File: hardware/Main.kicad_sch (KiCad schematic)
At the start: 1 part

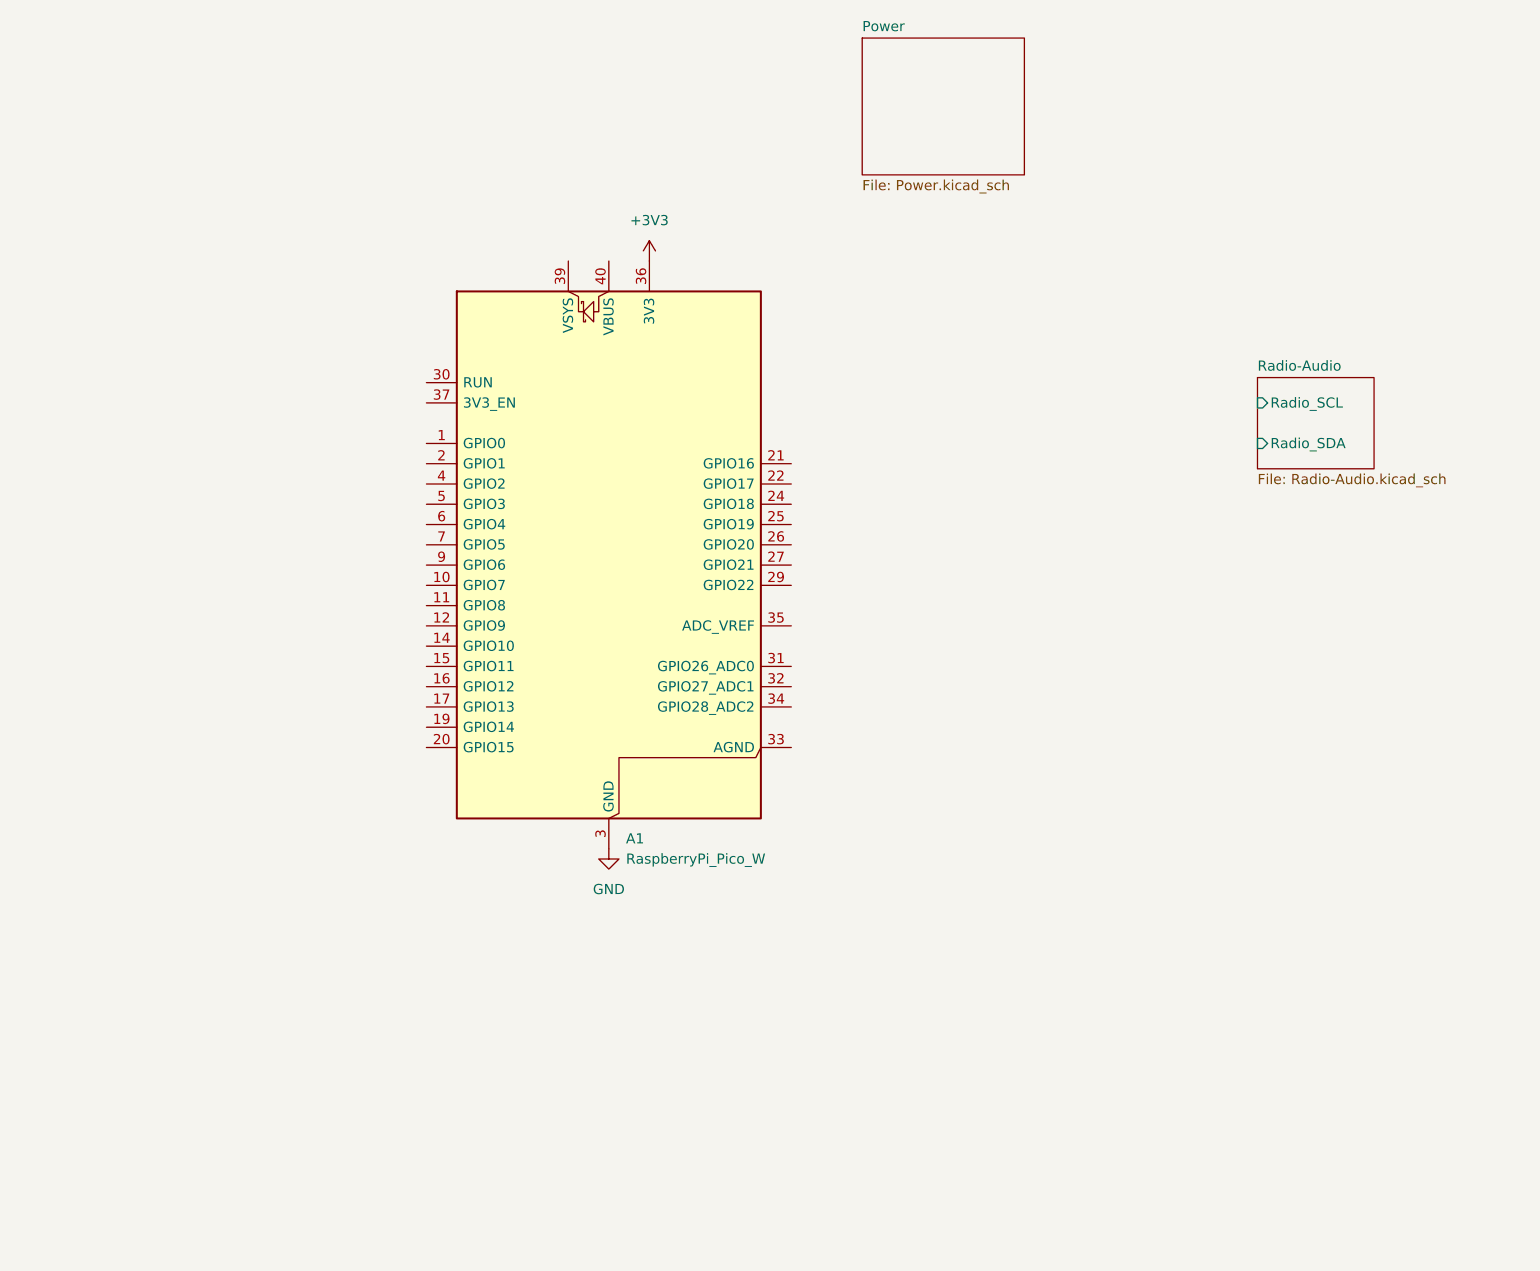
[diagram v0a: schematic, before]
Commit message: Added Radio Module to circuit
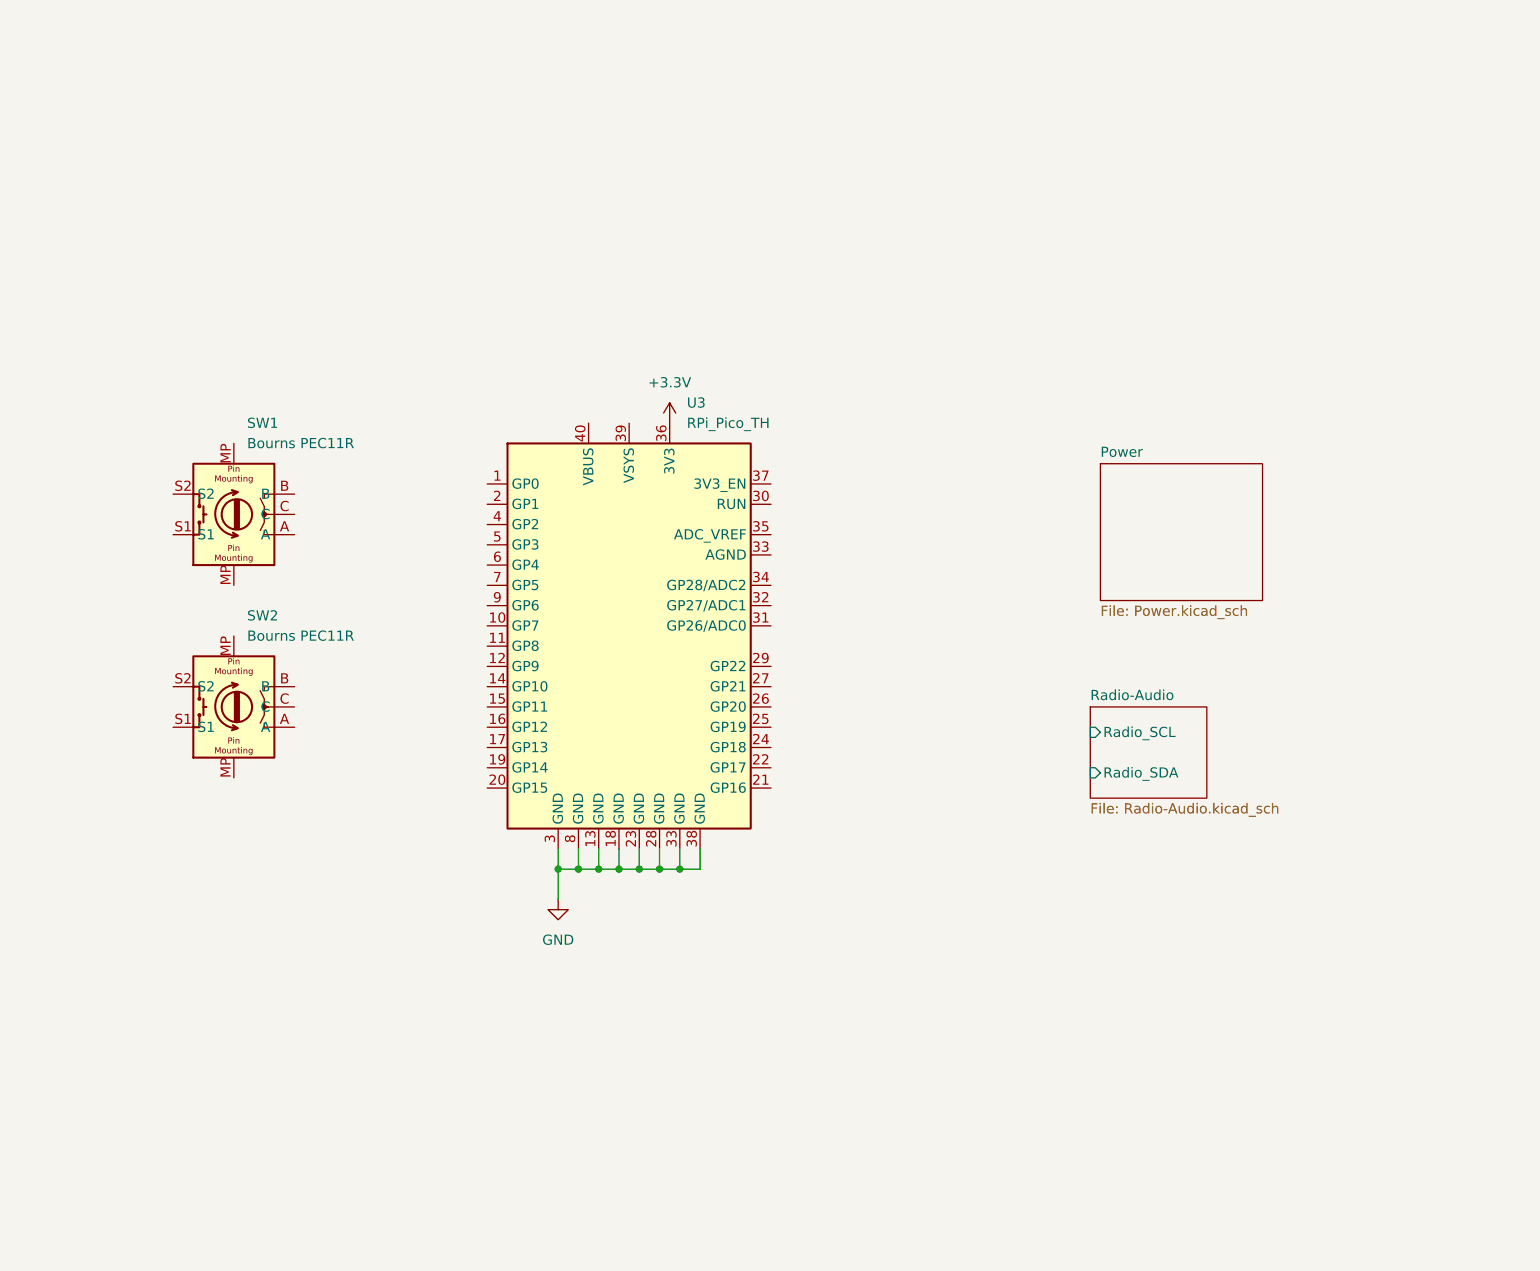
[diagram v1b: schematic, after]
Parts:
- removed A1: RaspberryPi_Pico_W, Module:RaspberryPi_Pico_Common_SMD, symbol MCU_Module:RaspberryPi_Pico_W
- added SW1, SW2: Bourns PEC11R, Rotary_Encoder:RotaryEncoder_Alps_EC12E-Switch_Vertical_H20mm, symbol ECE:Bourns PEC11R
- added U3: RPi_Pico_TH, ECE:RPi_Pico_TH, symbol ECE:RPi_Pico_TH
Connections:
- net GND: now also U3.13 (GND), U3.18 (GND), U3.23 (GND), U3.28 (GND), U3.3 (GND), U3.33 (AGND), U3.38 (GND), U3.8 (GND)
- new net +3.3V: U3.36 (3V3)

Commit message: Updated Encoder Circuit/Code
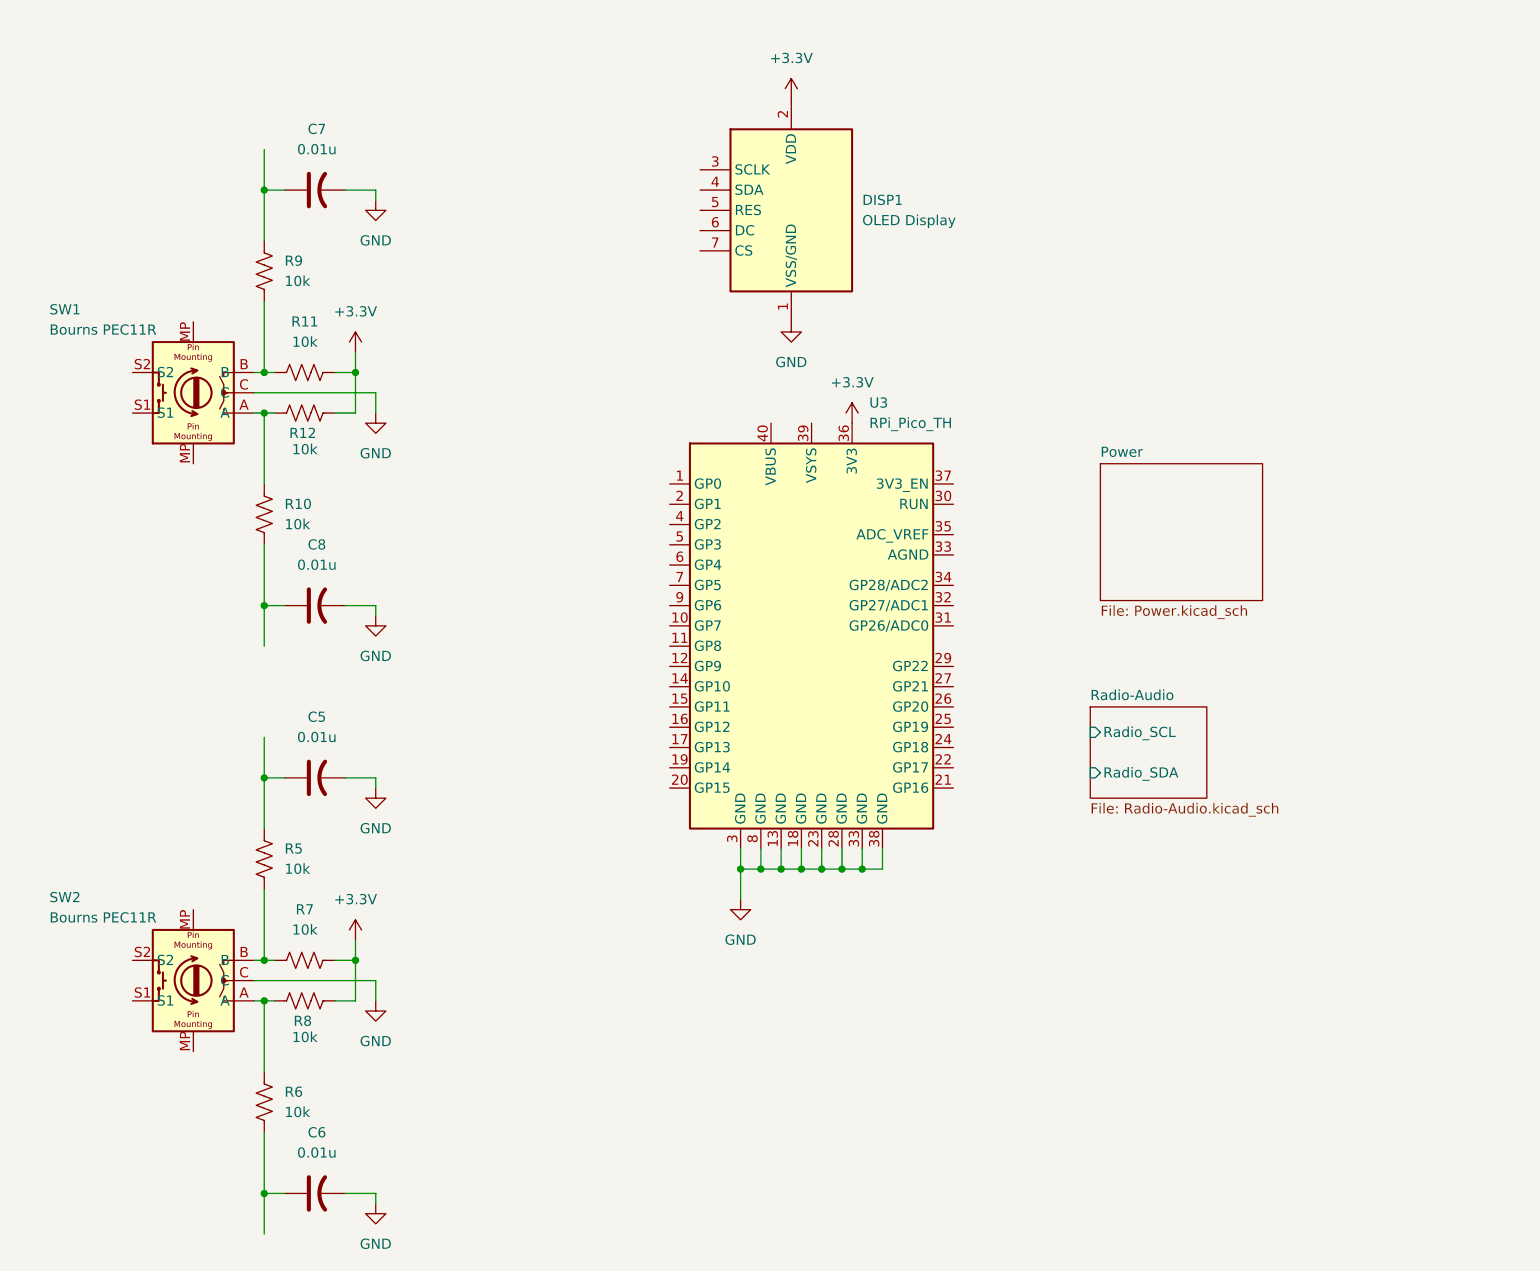
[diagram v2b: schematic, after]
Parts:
- added C5, C6, C7, C8: 0.01u, symbol Device:C_US
- added DISP1: OLED Display, symbol ECE:OLED Display
- added R10, R11, R12, R5, R6, R7, R8, R9: 10k, symbol Device:R_US
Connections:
- net +3.3V: now also DISP1.2 (VDD), R11.2, R12.2, R7.2, R8.2
- net GND: now also SW1.C, SW2.C, C5.2, C6.2, C7.2, C8.2, DISP1.1 (VSS/GND)
- net at SW2.A: now also R6.2, R8.1
- net at SW2.B: now also R5.1, R7.1
- net at SW1.A: now also R10.2, R12.1
- net at SW1.B: now also R11.1, R9.1
- new net: C7.1, R9.2
- new net: C8.1, R10.1
- new net: C6.1, R6.1
- new net: C5.1, R5.2
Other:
- moved on the sheet: U3

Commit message: Assigned Pinout to Subsystems
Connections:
- net Radio-Audio/Radio_SCL: now also U3.22 (GP17)
- net Radio-Audio/Radio_SDA: now also U3.21 (GP16)
- net ENC2B: now reaches C7.1, R9.2
- net ENC2B: now also U3.1 (GP0)
- net DISP_SCLK: now reaches DISP1.3 (SCLK)
- net DISP_SCLK: now also U3.4 (GP2)
- net DISP_SDA: now reaches DISP1.4 (SDA)
- net DISP_SDA: now also U3.5 (GP3)
- net DISP_RES: now reaches DISP1.5 (RES)
- net DISP_RES: now also U3.9 (GP6)
- net DISP_DC: now reaches DISP1.6 (DC)
- net DISP_DC: now also U3.10 (GP7)
- net DISP_CS: now reaches DISP1.7 (CS)
- net DISP_CS: now also U3.7 (GP5)
- net ENC1B: now reaches U3.19 (GP14)
- net ENC1B: now also C5.1, R5.2
- net ENC2A: now reaches U3.2 (GP1)
- net ENC2A: now also C8.1, R10.1
- net ENC1A: now reaches U3.20 (GP15)
- net ENC1A: now also C6.1, R6.1
- no-connect marks 0 -> 13

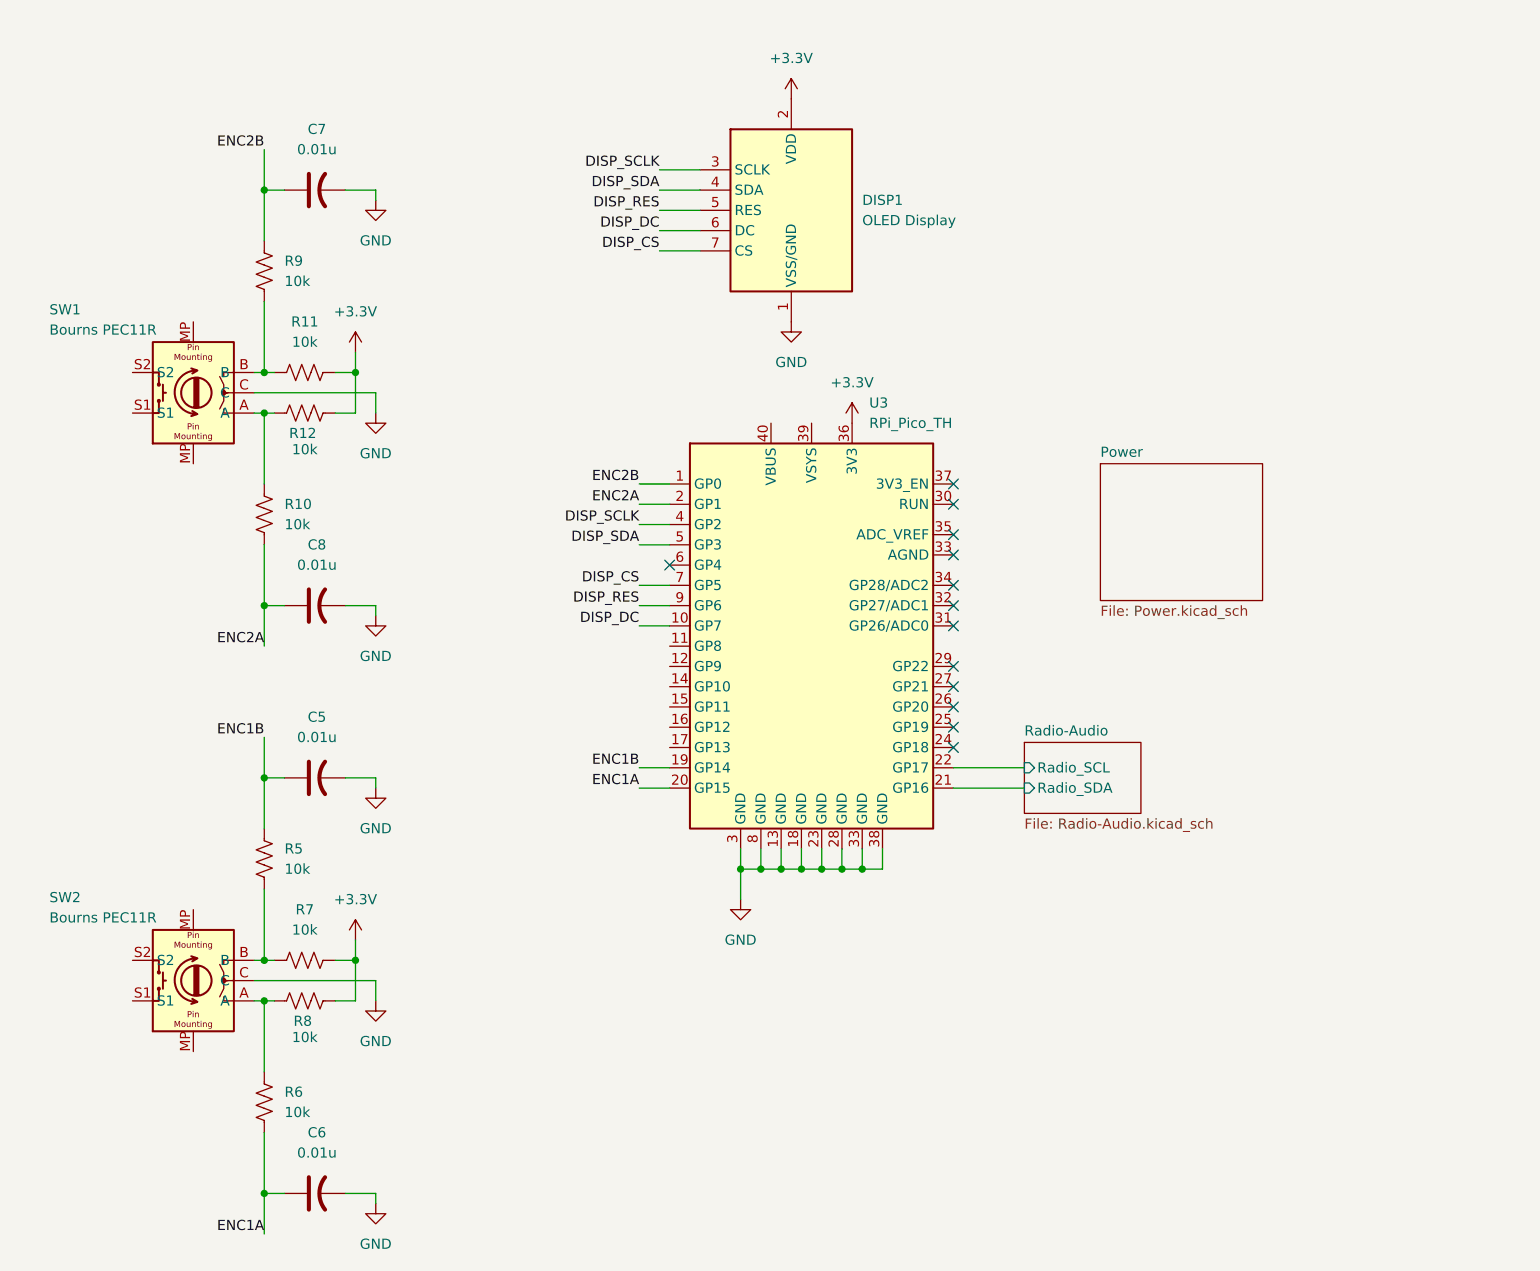
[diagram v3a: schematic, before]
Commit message: Powerchain
Powerchain first draft done
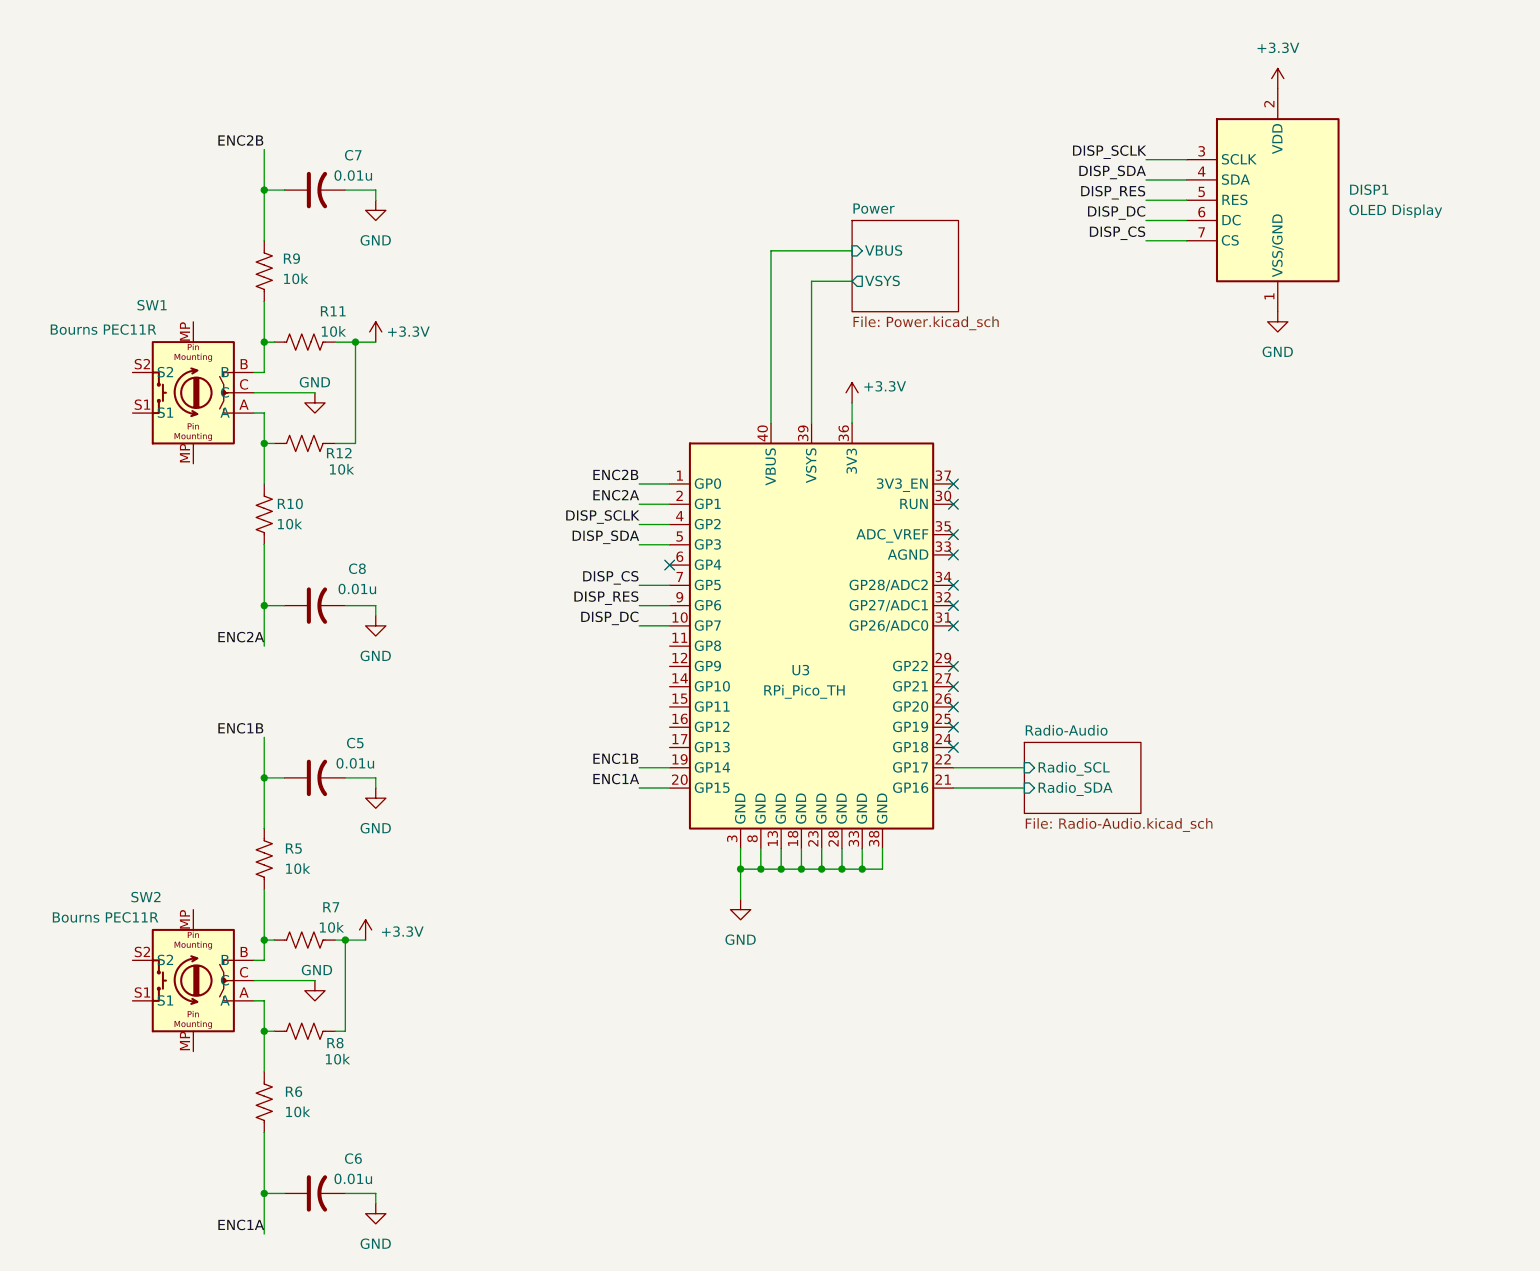
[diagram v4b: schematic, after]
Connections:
- net Power/VSYS: now reaches U3.39 (VSYS)
- net Power/VBUS: now reaches U3.40 (VBUS)
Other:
- sheet Power ports: added VBUS, VSYS; removed none
- moved on the sheet: DISP1, R11, R12, R7, R8

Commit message: Added Button circuit
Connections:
- net ENC1A: now also U3.19 (GP14); no longer U3.20 (GP15)
- net ENC1B: now also U3.20 (GP15); no longer U3.19 (GP14)
- net ENC2A: now also U3.1 (GP0); no longer U3.2 (GP1)
- net ENC2B: now also U3.2 (GP1); no longer U3.1 (GP0)
- net GND: now also SW1.MP, SW1.S1, SW2.MP, SW2.S1
- net ENC1_BTN: now reaches U3.27 (GP21)
- net ENC1_BTN: now also SW2.S2
- net ENC2_BTN: now reaches U3.29 (GP22)
- net ENC2_BTN: now also SW1.S2
- net Power/VSYS renamed +5V
- no-connect marks 13 -> 17
